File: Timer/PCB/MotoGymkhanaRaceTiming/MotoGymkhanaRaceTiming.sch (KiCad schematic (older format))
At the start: 42 parts, among them U1 LM2577T-ADJ_NOPB, U2 PC817, U3 PC817

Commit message: Issue 19: Starting schematics for carrier PCB for rider ID
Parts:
- U1: symbol MotoGymkhanaRaceTiming-rescue:LM2577T-ADJ_NOPB-2020-05-24_13-28-23 -> MotoGymkhanaRaceTiming-rescue:LM2577T-ADJ_NOPB-2020-05-24_13-28-23-MotoGymkhanaRaceTiming-rescue
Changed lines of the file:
@@
 Connection ~ 6300 3050
 $Comp
-L MotoGymkhanaRaceTiming-rescue:LM2577T-ADJ_NOPB-2020-05-24_13-28-23 U1
+L MotoGymkhanaRaceTiming-rescue:LM2577T-ADJ_NOPB-2020-05-24_13-28-23-MotoGymkhanaRaceTiming-rescue U1
 U 1 1 5ED0DA73
 P 850 6700

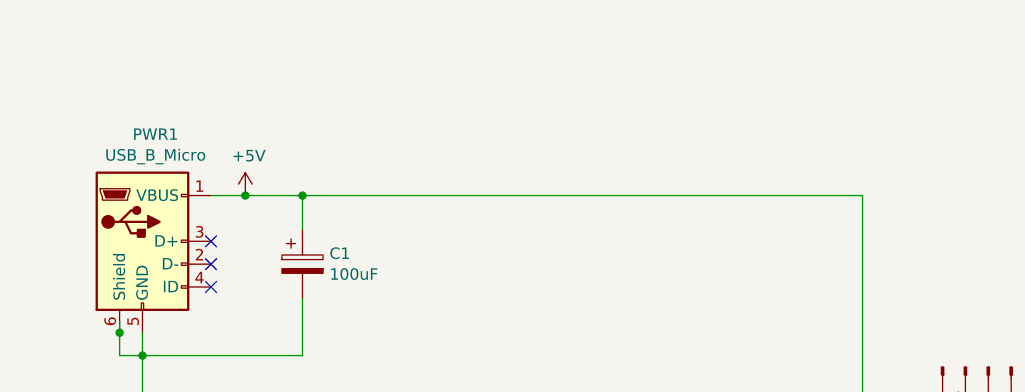
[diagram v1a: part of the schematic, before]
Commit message: Starting issue #29: Carrier PCB for central unit and improved PCBs for other units, as ordered.
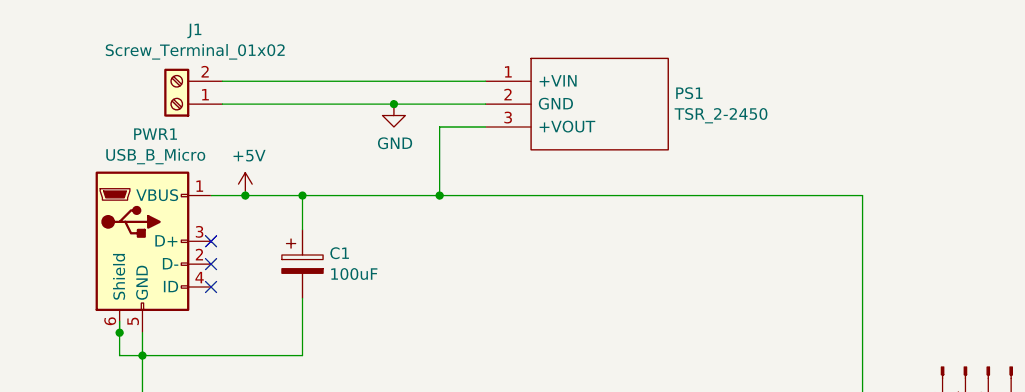
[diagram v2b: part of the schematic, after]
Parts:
- added J1: Screw_Terminal_01x02, Connector_Phoenix_MSTB:PhoenixContact_MSTBA_2,5_2-G_1x02_P5.00mm_Horizontal, symbol Connector:Screw_Terminal_01x02
- added PS1: TSR_2-2450, MotoGymkhanaRaceTiming:TSR-2, symbol TSR_2-2450:TSR_2-2450
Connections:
- net +5V: now also PS1.3 (+VOUT)
- net GND: now also J1.1 (Pin_1), PS1.2 (GND)
- new net: J1.2 (Pin_2), PS1.1 (+VIN)
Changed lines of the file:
@@
 Connection ~ 1950 1350
 Wire Wire Line
-	1950 1350 4400 1350
+	1950 1350 2550 1350
 Wire Wire Line
 	1950 1800 1950 2050
@@
 Text Label 800  7250 3    50   ~ 0
 12V
+$Comp
+L TSR_2-2450:TSR_2-2450 PS1
+U 1 1 605B9C68
+P 2750 850
+F 0 "PS1" H 3578 796 50  0000 L CNN
+F 1 "TSR_2-2450" H 3578 705 50  0000 L CNN
+F 2 "MotoGymkhanaRaceTiming:TSR-2" H 3600 950 50  0001 L CNN
+F 3 "https://componentsearchengine.com/Datasheets/1/TSR 2-2450.pdf" H 3600 850 50  0001 L CNN
+F 4 "Switching Regulator 5Vout 2A TRACOPOWER Switching Regulator, 6.5  36V dc Input, 5V dc Output, Maximum of 2A" H 3600 750 50  0001 L CNN "Description"
+F 5 "" H 3600 650 50  0001 L CNN "Height"
+F 6 "Traco Power" H 3600 550 50  0001 L CNN "Manufacturer_Name"
+F 7 "TSR 2-2450" H 3600 450 50  0001 L CNN "Manufacturer_Part_Number"
+F 8 "495-TSR2-2450" H 3600 350 50  0001 L CNN "Mouser Part Number"
+F 9 "https://www.mouser.co.uk/ProductDetail/TRACO-Power/TSR-2-2450/?qs=NtE2QagKf6RzknAolzm%2FTQ%3D%3D" H 3600 250 50  0001 L CNN "Mouser Price/Stock"
+F 10 "" H 3600 150 50  0001 L CNN "Arrow Part Number"
+F 11 "" H 3600 50  50  0001 L CNN "Arrow Price/Stock"
+	1    2750 850
+	1    0    0    -1
+$EndComp
+Wire Wire Line
+	2750 1050 2550 1050
+Wire Wire Line
+	2550 1050 2550 1350
+Connection ~ 2550 1350
+Wire Wire Line
+	2550 1350 4400 1350
+$Comp
+L power:GND #PWR0110
+U 1 1 605C7356
+P 2350 950
+F 0 "#PWR0110" H 2350 700 50  0001 C CNN
+F 1 "GND" H 2355 777 50  0000 C CNN
+F 2 "" H 2350 950 50  0001 C CNN
+F 3 "" H 2350 950 50  0001 C CNN
+	1    2350 950
+	1    0    0    -1
+$EndComp
+Wire Wire Line
+	2350 950  2750 950
+$Comp
+L Connector:Screw_Terminal_01x02 J1
+U 1 1 605D42A6
+P 1400 950
+F 0 "J1" H 1318 625 50  0000 C CNN
+F 1 "Screw_Terminal_01x02" H 1318 716 50  0000 C CNN
+F 2 "Connector_Phoenix_MSTB:PhoenixContact_MSTBA_2,5_2-G_1x02_P5.00mm_Horizontal" H 1400 950 50  0001 C CNN
+F 3 "~" H 1400 950 50  0001 C CNN
+	1    1400 950
+	-1   0    0    1
+$EndComp
+Wire Wire Line
+	1600 950  2350 950
+Connection ~ 2350 950
+Wire Wire Line
+	1600 850  2750 850
 $EndSCHEMATC
